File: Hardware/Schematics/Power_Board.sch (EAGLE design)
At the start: 64 parts, among them IC3 74AC373DW, J1 1X2-3.5MM, J2 1X2-3.5MM, J4 1X2-3.5MM, Q1 BSL207SP, Q2 BSL207SP, Q3 MOSFET-NCHANNELSMD, Q8 4.096MHz, U1 ESP-32S

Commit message: Created new logicboard with isolation from HV side.
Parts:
- removed BUTTON1, BUTTON2, BUTTON3: (no value), pinhead:PINHD-1X3
- removed C1, C17, C18, C2, C3, C4, C5, C6, C7: 100nF, rcl:C-EUC1206
- removed FLASH, RESET: -, switch-omron:10-XX
- removed IC3: 74AC373DW, 74xx-eu:74AC373DW
- removed J1: 1X2-3.5MM, adafruit:1X2-3.5MM
- removed JTAG, UART: -, pinhead:PINHD-1X4
- removed Q4, Q5, Q6: (no value), adafruit:MOSFET-NREFLOW
- removed R1, R17, R2: 10K, rcl:R-EU_R0805
- removed R20, R22, R7: 100, rcl:R-EU_R0805
- removed U$11, U$4, U$6, U$7: ADUM1410, PowerSocket:ADUM1410
- removed U$8: HLK-PM03, PowerSocket:HLK-PM03
- removed U1: ESP-32S, esp32:ESP-32S
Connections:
- removed net BUTTON1: BUTTON1.3, U1.IO21
- removed net BUTTON2: BUTTON2.3, U1.IO18
- removed net BUTTON3: BUTTON3.3, U1.IO17
- removed net CS2: U$7.VOA
- removed net CS3: U$11.VOD
- removed net FLASH: FLASH.P, FLASH.P1, R2.2, U1.IO0
- removed net GND: C1.2, C17.2, C2.2, C4.2, C7.2, FLASH.S, FLASH.S1, IC3A.4D, IC3A.5D, IC3A.6D, IC3A.7D, IC3A.8D, IC3A.OC, Q4.S, Q5.S, Q6.S, R17.2, RESET.S, RESET.S1, U$11.DISABLE, U$11.GND1@1, U$11.GND1@2, U$4.DISABLE, U$4.GND1@1, U$4.GND1@2, U$6.GND2@1, U$6.GND2@2, U$7.DISABLE, U$7.GND1@1, U$7.GND1@2, U$8.-VO, U1.GND@1, U1.GND@2, U1.GND@3, U1.GND@4, U1.IO2, UART.1
- removed net LED1: Q5.G, U1.IO19
- removed net LED1_SWITCHED: Q5.D, R7.2
- removed net LED2: Q4.G, U1.IO5
- removed net LED2_SWITCHED: Q4.D, R20.2
- removed net LED3: Q6.G, U1.IO16
- removed net LED3_SWITCHED: Q6.D, R22.2
- removed net N$1: J1.2, U$8.AC1
- removed net N$11: BUTTON3.2, R22.1
- removed net N$13: J1.1, U$8.AC2
- removed net N$14: U$6.DISABLE, U$6.GND1@2
- removed net N$2: JTAG.1, U1.IO15
- removed net N$24: U$6.VID
- removed net N$27: U$6.VIC
- removed net N$28: U$6.VIB
- removed net N$29: U$6.VOA
- removed net N$3: JTAG.2, U1.IO13
- removed net N$31: U$6.VOB
- removed net N$32: IC3A.ENC, R17.1, U1.IO33
- removed net N$33: IC3A.1D, U1.IO27
- removed net N$34: IC3A.2D, U1.IO26
- removed net N$35: IC3A.3D, U1.IO25
- removed net N$36: U$6.VOC
- removed net N$37: U$6.VOD
- removed net N$39: U$6.VE2
- removed net N$4: JTAG.3, U1.IO12
- removed net N$40: U$4.VID
- removed net N$41: U$4.VIC
- removed net N$45: U$4.VIB
- removed net N$49: U$4.VIA
- removed net N$5: JTAG.4, U1.IO14
- removed net N$51: U$7.VIA
- removed net N$52: U$7.VIB
- removed net N$53: U$7.VIC
- removed net N$54: U$11.VID, U$7.VID
- removed net N$55: U$11.VIC
- removed net N$66: R1.1, RESET.P, RESET.P1, U1.EN
- removed net N$7: BUTTON2.2, R20.1
- removed net N$70: U1.U0TXD, UART.2
- removed net N$77: U1.U0RXD, UART.3
- removed net N$9: BUTTON1.2, R7.1
- removed net RELAY1: U$4.VOB
- removed net RELAY2: U$4.VOC
- removed net RELAY3: U$4.VOD
- removed net VCC: BUTTON1.1, BUTTON2.1, BUTTON3.1, C1.1, C17.1, C2.1, C4.1, C7.1, R1.2, R2.1, U$11.VDD1, U$4.VDD1, U$6.VDD2, U$7.VDD1, U$8.+VO, U1.3V3, UART.4
- net +5V: no longer C18.1, C3.1, C5.1, C6.1, U$11.VDD2, U$4.VDD2, U$6.VDD1, U$7.VDD2
- net CS1: no longer U$7.VOB
- net GND1: no longer C18.2, C3.2, C5.2, C6.2, U$11.GND2@1, U$11.GND2@2, U$4.GND2@1, U$4.GND2@2, U$6.GND1@1, U$7.GND2@1, U$7.GND2@2
- net RELAY_SUPL_CTRL: no longer U$4.VOA
- net RESET: no longer U$11.VOC
- net SCLK: no longer U$7.VOC
- net SDI: no longer U$7.VOD
- net SDO: no longer U$6.VIA
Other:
- moved on the sheet: JP1

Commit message: Power board schematic mostly done.
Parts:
- added C1, C19, C2, C20, C21, C3: 100nF, rcl:C-EUC1206
- added C17, C22, C23, C25, C26, C4, C5, C7: 220nF, rcl:C-EUC1206
- added C18, C24, C27, C6: 22nF, rcl:C-EUC1206
- added C28: (no value), rcl:CPOL-EUE3.5-8
- added D1, D2: (no value), diode:DIODE-DO-214AC
- added J1, J3: 1X2-3.5MM, adafruit:1X2-3.5MM
- added Q4, Q6: (no value), adafruit:MOSFET-NREFLOW
- added Q5, Q9: 4.096MHz, crystal:CRYSTALHC49U70
- added R1: 1K, resistor:R-EU_R0805
- added R11, R13, R14, R17, R19, R20: 1K, rcl:R-EU_R0805
- added R12, R18: 12m, rcl:R-EU_R2512
- added R15, R2: 1M, rcl:R-EU_R0805
- added R16, R7: 560, rcl:R-EU_R1206
- added U$10, U$15: POWER_SOCKET_EU, PowerSocket:POWER_SOCKET_EU
- added U$11, U$13, U$6, U$7: RELAYPTH, SRD-05VDC-SL-C:RELAYPTH
- added U$14, U$8: CS5463, PowerSocket:CS5463
- added U$4: PCF8574AT, i2c:PCF8574AT
- JP1: device pinhead:PINHD-2X16/90 -> pinhead:PINHD-2X9/90
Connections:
- removed net +5V: C10.1, C9.1, Q2.S, R3.2, U$1.IN+, U$5.+VO, U$9.VA+, U$9.VD+
- removed net GND1: C10.2, C11.2, C12.1, C14.2, C15.1, C8.2, C9.2, Q3.S, Q7.S, U$1.GND, U$1.GND2, U$5.-VO, U$9.AGND, U$9.DGND, U$9.MODE
- new net AC1: J4.1, U$5.AC1
- new net AC2: J4.2, U$5.AC2
- new net CS2: JP1.14, U$8.CS
- new net CS3: JP1.15, U$14.CS
- new net GND: C1.2, C10.2, C11.2, C12.1, C14.2, C15.1, C17.1, C19.2, C2.2, C20.2, C21.2, C22.2, C23.1, C25.2, C26.1, C28.-, C3.2, C4.2, C5.1, C7.2, C8.2, C9.2, JP1.1, JP1.10, JP1.13, JP1.18, JP1.6, Q3.S, Q4.S, Q6.S, Q7.S, U$1.GND, U$1.GND2, U$14.AGND, U$14.DGND, U$14.MODE, U$4IC$1.A0, U$4IC$1.A1, U$4IC$1.A2, U$5.-VO, U$8.AGND, U$8.DGND, U$8.MODE, U$9.AGND, U$9.DGND, U$9.MODE
- new net INT1: U$4IC$1.P5, U$9.INT
- new net INT2: U$4IC$1.P6, U$8.INT
- new net INT3: U$14.INT, U$4IC$1.P7
- new net N$1: D1.A, Q4.D, U$6.COIL0, U$7.COIL0
- new net N$11: C19.1, U$14.VREFIN, U$14.VREFOUT
- new net N$13: C25.1, C27.1, R20.2, U$14.IIN+
- new net N$14: Q9.2, U$14.XIN
- new net N$19: R16.2, R17.1, R18.1, R20.1, U$11.SWCOMMON
- new net N$2: Q5.1, U$8.XOUT
- new net N$24: C26.2, C27.2, R19.2, U$14.IIN-
- new net N$3: C1.1, U$8.VREFIN, U$8.VREFOUT
- new net N$4: C18.1, C7.1, R14.2, U$8.IIN+
- new net N$5: Q5.2, U$8.XIN
- new net N$7: C17.2, C18.2, R13.2, U$8.IIN-
- new net N$9: Q9.1, U$14.XOUT
- new net NULL2: J1.1, R2.1, U$7.SWCOMMON
- new net NULL2_OUT: U$10.AC1, U$7.SWCLOSE
- new net NULL3: J3.1, R15.1, U$13.SWCOMMON
- new net NULL3_OUT: U$13.SWCLOSE, U$15.AC1
- new net PC8574_INT: JP1.3, R1.1, U$4IC$1./INT
- new net PHASE2: J1.2, R12.2, R13.1
- new net PHASE2_OUT: U$10.AC2, U$6.SWCLOSE
- new net PHASE3: J3.2, R18.2, R19.1
- new net PHASE3_OUT: U$11.SWCLOSE, U$15.AC2
- new net RELAY1: Q7.G, U$4IC$1.P1
- new net RELAY2: Q4.G, U$4IC$1.P2
- new net RELAY3: Q6.G, U$4IC$1.P3
- new net SCL: JP1.5, U$4IC$1.SCL
- new net SDA: JP1.8, U$4IC$1.SDA
- new net VCC: C10.1, C2.1, C20.1, C21.1, C28.+, C3.1, C9.1, JP1.16, JP1.17, JP1.2, JP1.7, Q2.S, R1.2, R3.2, U$1.IN+, U$14.VA+, U$14.VD+, U$5.+VO, U$8.VA+, U$8.VD+, U$9.VA+, U$9.VD+
- new net VIN+2: C5.2, C6.2, R2.2, R7.1, U$8.VIN+
- new net VIN+3: C23.2, C24.2, R15.2, R16.1, U$14.VIN+
- new net VIN-2: C4.1, C6.1, R11.2, U$8.VIN-
- new net VIN-3: C22.1, C24.1, R17.2, U$14.VIN-
- net CS1: now also JP1.11
- net N$6: now also R11.1, R12.1, R14.1, R7.2, U$6.SWCOMMON; no longer J4.2, U$5.AC1
- net N$8: now also D2.A, Q6.D, U$11.COIL0, U$13.COIL0; no longer J4.1, U$5.AC2
- net RELAY_SUPL_CTRL: now also U$4IC$1.P0
- net RELAY_SUPPLY: now also D1.C, D2.C, U$11.COIL1, U$13.COIL1, U$6.COIL1, U$7.COIL1
- net RESET: now also U$14.RESET, U$4IC$1.P4, U$8.RESET
- net SCLK: now also JP1.12, U$14.SCLK, U$8.SCLK
- net SDI: now also JP1.9, U$14.SDI, U$8.SDI
- net SDO: now also JP1.4, U$14.SDO, U$8.SDO
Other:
- moved on the sheet: Q1, Q2, Q3, R3

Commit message: Relay board placement mostly done. Routing ~50% done.
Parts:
- added C29: 100nF, rcl:C-EUC0805
- C1, C10, C11, C12, C13, C14, C15, C16, C17, C18, C19, C2, C20, C21, C22, C23, C24, C25, C26, C27, C3, C4, C5, C6, C7, C8, C9: device rcl:C-EUC1206 -> rcl:C-EUC0805
- C28: device rcl:CPOL-EUE3.5-8 -> rcl:CPOL-EUE5-6
- Q1, Q2: value BSL207SP -> MOSFET-PCHANNEL_SOT23-3; device transistor-fet:BSL207SP -> Simplex-DiscreteSemi:MOSFET-PCHANNEL_SOT23-3
- U$11, U$13, U$2, U$3, U$6, U$7: device SRD-05VDC-SL-C:RELAYPTH -> PowerSocket:RELAYPTH
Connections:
- removed net AC1: J4.1, U$5.AC1
- removed net AC2: J4.2, U$5.AC2
- new net NULL_PS: J4.1, U$5.AC2
- net GND: now also C29.1
- net N$19: now also U$11.SWOPEN; no longer U$11.SWCOMMON
- net N$26: now also U$3.SWOPEN; no longer U$2.SWCOMMON
- net N$6: now also U$6.SWOPEN; no longer U$6.SWCOMMON
- net NULL1: now also U$2.SWOPEN; no longer U$3.SWCOMMON
- net NULL1_OUT: now also U$2.SWCOMMON; no longer U$3.SWCLOSE
- net NULL2: now also U$7.SWOPEN; no longer U$7.SWCOMMON
- net NULL2_OUT: now also U$7.SWCOMMON; no longer U$7.SWCLOSE
- net NULL3: now also U$13.SWOPEN; no longer U$13.SWCOMMON
- net NULL3_OUT: now also U$13.SWCOMMON; no longer U$13.SWCLOSE
- net PHASE1: now also J4.2, U$5.AC1; no longer J2.2
- net PHASE1_OUT: now also U$3.SWCOMMON; no longer U$2.SWCLOSE
- net PHASE2: now also J2.2; no longer J1.2
- net PHASE2_OUT: now also U$6.SWCOMMON; no longer U$6.SWCLOSE
- net PHASE3: now also J1.2; no longer J3.2
- net PHASE3_OUT: now also U$11.SWCOMMON; no longer U$11.SWCLOSE
- net VCC: now also C29.2

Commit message: Power board routing done. Still missing adjustments of soldermask and silkscreen on both powerboard and logic board.
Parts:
- R1: value 1K -> 2.5K
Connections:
- net INT1: now also U$4IC$1.P4; no longer U$4IC$1.P5
- net N$13: now also U$14.IIN-; no longer U$14.IIN+
- net N$24: now also U$14.IIN+; no longer U$14.IIN-
- net N$30: now also U$9.IIN+; no longer U$9.IIN-
- net N$4: now also U$8.IIN-; no longer U$8.IIN+
- net N$42: now also U$9.IIN-; no longer U$9.IIN+
- net N$7: now also U$8.IIN+; no longer U$8.IIN-
- net RELAY1: now also U$4IC$1.P3; no longer U$4IC$1.P1
- net RELAY3: now also U$4IC$1.P1; no longer U$4IC$1.P3
- net RESET: now also U$4IC$1.P5; no longer U$4IC$1.P4
- net VIN+1: now also U$9.VIN-; no longer U$9.VIN+
- net VIN+2: now also U$8.VIN-; no longer U$8.VIN+
- net VIN+3: now also U$14.VIN-; no longer U$14.VIN+
- net VIN-1: now also U$9.VIN+; no longer U$9.VIN-
- net VIN-2: now also U$8.VIN+; no longer U$8.VIN-
- net VIN-3: now also U$14.VIN+; no longer U$14.VIN-

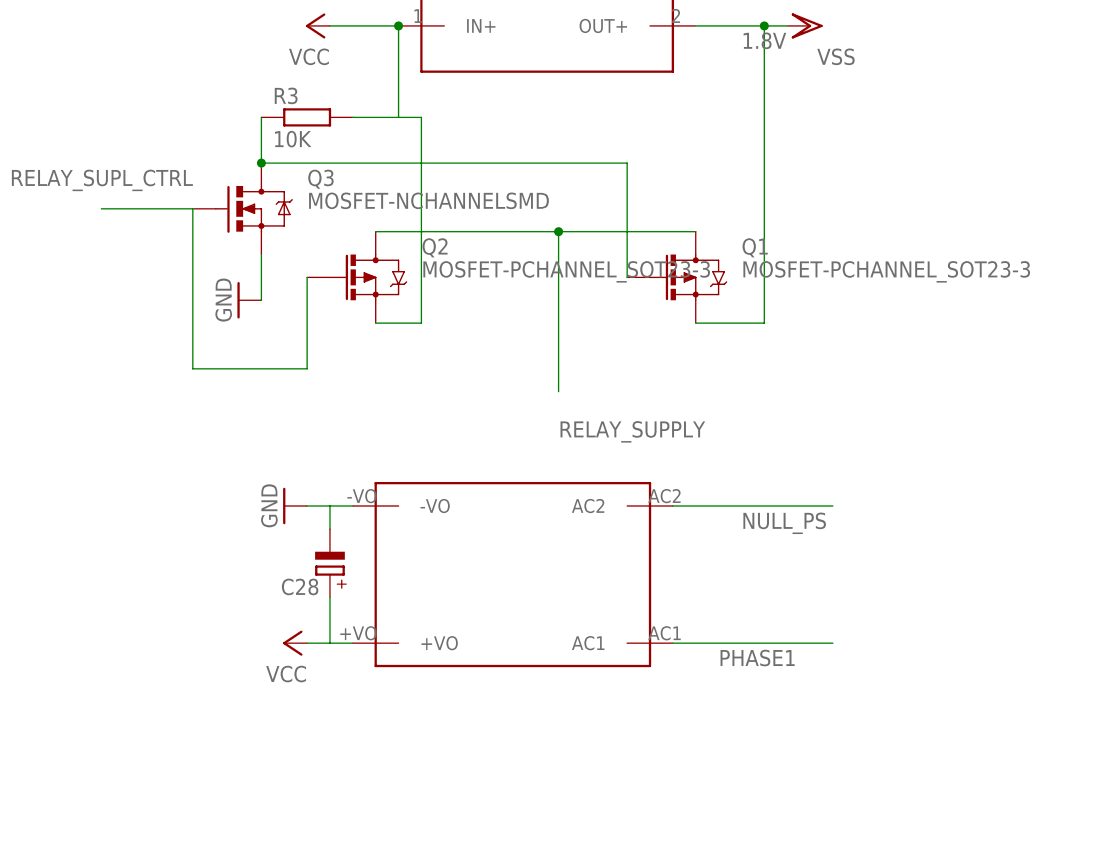
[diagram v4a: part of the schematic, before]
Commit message: Values and names fixed in silkscreen for powerboard. Slots added to powerboard.
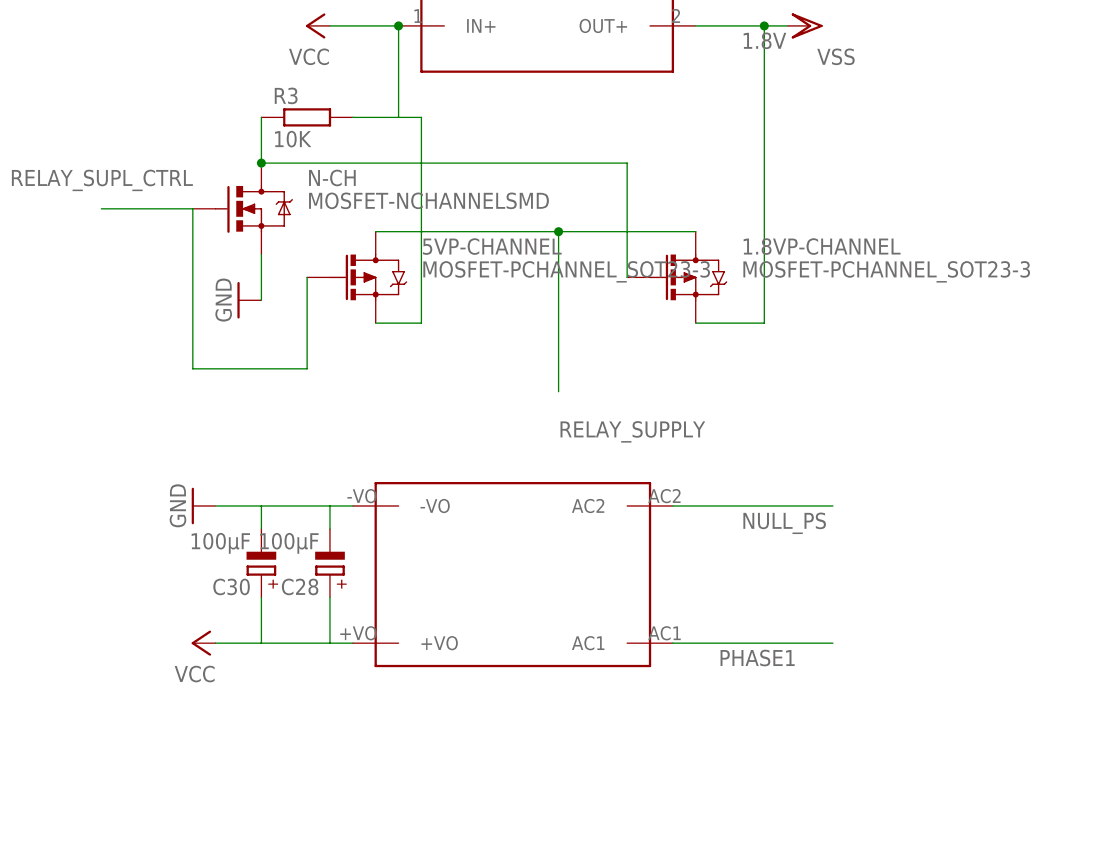
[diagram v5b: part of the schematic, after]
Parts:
- added C30: 100µF, rcl:CPOL-EUE5-6
- C28: value (none) -> 100µF
- renumbered Q1 to 1.8VP-CHANNEL, Q2 to 5VP-CHANNEL, Q3 to N-CH
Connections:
- net GND: now also C30.-
- net VCC: now also C30.+
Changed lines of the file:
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@@
 <part name="SUPPLY2" library="supply1" library_urn="urn:adsk.eagle:library:371" deviceset="GND" device=""/>
 <part name="SUPPLY3" library="supply1" library_urn="urn:adsk.eagle:library:371" deviceset="GND" device=""/>
-<part name="Q1" library="Simplex-DiscreteSemi" deviceset="MOSFET-PCHANNEL" device="_SOT23-3"/>
-<part name="Q2" library="Simplex-DiscreteSemi" deviceset="MOSFET-PCHANNEL" device="_SOT23-3"/>
-<part name="Q3" library="fets" deviceset="MOSFET-NCHANNEL" device="SMD"/>
+<part name="1.8VP-CHANNEL" library="Simplex-DiscreteSemi" deviceset="MOSFET-PCHANNEL" device="_SOT23-3"/>
+<part name="5VP-CHANNEL" library="Simplex-DiscreteSemi" deviceset="MOSFET-PCHANNEL" device="_SOT23-3"/>
+<part name="N-CH" library="fets" deviceset="MOSFET-NCHANNEL" device="SMD"/>
 <part name="R3" library="resistor" library_urn="urn:adsk.eagle:library:348" deviceset="R-EU_" device="R0805" value="10K"/>
 <part name="SUPPLY4" library="supply1" library_urn="urn:adsk.eagle:library:371" deviceset="GND" device=""/>
@@
 <part name="J3" library="adafruit" deviceset="1X2" device="-3.5MM"/>
 <part name="U$15" library="PowerSocket" deviceset="POWER_SOCKET_EU" device=""/>
-<part name="C28" library="rcl" library_urn="urn:adsk.eagle:library:334" deviceset="CPOL-EU" device="E5-6"/>
+<part name="C28" library="rcl" library_urn="urn:adsk.eagle:library:334" deviceset="CPOL-EU" device="E5-6" value="100µF"/>
 <part name="C29" library="rcl" deviceset="C-EU" device="C0805" value="100nF"/>
 <part name="SUPPLY29" library="supply1" library_urn="urn:adsk.eagle:library:371" deviceset="GND" device=""/>
+<part name="C30" library="rcl" library_urn="urn:adsk.eagle:library:334" deviceset="CPOL-EU" device="E5-6" value="100µF"/>
 </parts>
 <sheets>
@@
 <instance part="P+1" gate="VCC" x="53.34" y="190.5" rot="R90"/>
 <instance part="VSS1" gate="G$1" x="109.22" y="190.5" rot="R90"/>
-<instance part="P+6" gate="VCC" x="50.8" y="121.92" rot="R90"/>
-<instance part="SUPPLY1" gate="1" x="50.8" y="137.16" rot="R270"/>
+<instance part="P+6" gate="VCC" x="40.64" y="121.92" rot="R90"/>
+<instance part="SUPPLY1" gate="1" x="40.64" y="137.16" rot="R270"/>
 <instance part="U$1" gate="G$1" x="78.74" y="198.12"/>
 <instance part="SUPPLY2" gate="1" x="55.88" y="205.74" rot="R270"/>
 <instance part="SUPPLY3" gate="1" x="104.14" y="205.74" rot="R90"/>
-<instance part="Q1" gate="G$1" x="96.52" y="162.56"/>
-<instance part="Q2" gate="G$1" x="60.96" y="162.56"/>
-<instance part="Q3" gate="G$1" x="48.26" y="170.18"/>
+<instance part="1.8VP-CHANNEL" gate="G$1" x="96.52" y="162.56"/>
+<instance part="5VP-CHANNEL" gate="G$1" x="60.96" y="162.56"/>
+<instance part="N-CH" gate="G$1" x="48.26" y="170.18"/>
 <instance part="R3" gate="G$1" x="53.34" y="180.34"/>
 <instance part="SUPPLY4" gate="1" x="45.72" y="160.02" rot="R270"/>
@@
 <instance part="C29" gate="G$1" x="43.18" y="38.1" rot="R270"/>
 <instance part="SUPPLY29" gate="1" x="50.8" y="38.1" rot="R90"/>
+<instance part="C30" gate="G$1" x="48.26" y="129.54" rot="R180"/>
 </instances>
 <busses>
@@
 <wire x1="58.42" y1="121.92" x2="55.88" y2="121.92" width="0.1524" layer="91"/>
 <pinref part="C28" gate="G$1" pin="+"/>
-<wire x1="55.88" y1="121.92" x2="53.34" y2="121.92" width="0.1524" layer="91"/>
+<wire x1="55.88" y1="121.92" x2="48.26" y2="121.92" width="0.1524" layer="91"/>
+<wire x1="48.26" y1="121.92" x2="43.18" y2="121.92" width="0.1524" layer="91"/>
 <wire x1="55.88" y1="127" x2="55.88" y2="121.92" width="0.1524" layer="91"/>
+<pinref part="C30" gate="G$1" pin="+"/>
+<wire x1="48.26" y1="127" x2="48.26" y2="121.92" width="0.1524" layer="91"/>
 </segment>
 <segment>
@@
 <pinref part="P+1" gate="VCC" pin="VCC"/>
 <wire x1="63.5" y1="190.5" x2="55.88" y2="190.5" width="0.1524" layer="91"/>
-<pinref part="Q2" gate="G$1" pin="S"/>
+<pinref part="5VP-CHANNEL" gate="G$1" pin="S"/>
 <junction x="63.5" y="190.5"/>
 <pinref part="R3" gate="G$1" pin="2"/>
@@
 <wire x1="106.68" y1="190.5" x2="104.14" y2="190.5" width="0.1524" layer="91"/>
 <label x="101.6" y="187.96" size="1.778" layer="95"/>
-<pinref part="Q1" gate="G$1" pin="S"/>
+<pinref part="1.8VP-CHANNEL" gate="G$1" pin="S"/>
 <wire x1="104.14" y1="190.5" x2="96.52" y2="190.5" width="0.1524" layer="91"/>
 <wire x1="96.52" y1="157.48" x2="104.14" y2="157.48" width="0.1524" layer="91"/>
@@
 <net name="RELAY_SUPPLY" class="0">
 <segment>
-<pinref part="Q2" gate="G$1" pin="D"/>
+<pinref part="5VP-CHANNEL" gate="G$1" pin="D"/>
 <wire x1="60.96" y1="167.64" x2="81.28" y2="167.64" width="0.1524" layer="91"/>
 <wire x1="81.28" y1="167.64" x2="81.28" y2="149.86" width="0.1524" layer="91"/>
-<pinref part="Q1" gate="G$1" pin="D"/>
+<pinref part="1.8VP-CHANNEL" gate="G$1" pin="D"/>
 <wire x1="96.52" y1="167.64" x2="81.28" y2="167.64" width="0.1524" layer="91"/>
 <junction x="81.28" y="167.64"/>
@@
 <segment>
 <pinref part="R3" gate="G$1" pin="1"/>
-<pinref part="Q3" gate="G$1" pin="D"/>
+<pinref part="N-CH" gate="G$1" pin="D"/>
 <wire x1="48.26" y1="180.34" x2="48.26" y2="175.26" width="0.1524" layer="91"/>
-<pinref part="Q1" gate="G$1" pin="G"/>
+<pinref part="1.8VP-CHANNEL" gate="G$1" pin="G"/>
 <wire x1="48.26" y1="175.26" x2="88.9" y2="175.26" width="0.1524" layer="91"/>
 <wire x1="88.9" y1="175.26" x2="88.9" y2="162.56" width="0.1524" layer="91"/>
@@
 <net name="RELAY_SUPL_CTRL" class="0">
 <segment>
-<pinref part="Q3" gate="G$1" pin="G"/>
+<pinref part="N-CH" gate="G$1" pin="G"/>
 <wire x1="40.64" y1="170.18" x2="40.64" y2="152.4" width="0.1524" layer="91"/>
-<pinref part="Q2" gate="G$1" pin="G"/>
+<pinref part="5VP-CHANNEL" gate="G$1" pin="G"/>
 <wire x1="40.64" y1="152.4" x2="53.34" y2="152.4" width="0.1524" layer="91"/>
 <wire x1="53.34" y1="152.4" x2="53.34" y2="162.56" width="0.1524" layer="91"/>
@@
 <wire x1="58.42" y1="137.16" x2="55.88" y2="137.16" width="0.1524" layer="91"/>
 <pinref part="C28" gate="G$1" pin="-"/>
-<wire x1="55.88" y1="137.16" x2="53.34" y2="137.16" width="0.1524" layer="91"/>
+<wire x1="55.88" y1="137.16" x2="48.26" y2="137.16" width="0.1524" layer="91"/>
+<wire x1="48.26" y1="137.16" x2="43.18" y2="137.16" width="0.1524" layer="91"/>
 <wire x1="55.88" y1="134.62" x2="55.88" y2="137.16" width="0.1524" layer="91"/>
+<pinref part="C30" gate="G$1" pin="-"/>
+<wire x1="48.26" y1="134.62" x2="48.26" y2="137.16" width="0.1524" layer="91"/>
 </segment>
 <segment>
@@
 <segment>
 <pinref part="SUPPLY4" gate="1" pin="GND"/>
-<pinref part="Q3" gate="G$1" pin="S"/>
+<pinref part="N-CH" gate="G$1" pin="S"/>
 <wire x1="48.26" y1="160.02" x2="48.26" y2="165.1" width="0.1524" layer="91"/>
 </segment>
